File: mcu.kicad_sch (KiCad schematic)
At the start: 0 parts

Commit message: Added some components
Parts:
- added U301: STM32F413CHUx, Package_DFN_QFN:QFN-48-1EP_7x7mm_P0.5mm_EP5.6x5.6mm, symbol MCU_ST_STM32F4:STM32F413CHUx
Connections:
- new net: U301.23 (VSS), U301.35 (VSS), U301.47 (VSS), U301.49 (VSS)
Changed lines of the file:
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@@
 (kicad_sch (version 20230121) (generator eeschema)
   (paper "A4")
+  (symbol (lib_id "MCU_ST_STM32F4:STM32F413CHUx") (at 114.935 95.885 0) (unit 1)
+    (in_bom yes) (on_board yes) (dnp no) (fields_autoplaced)
+    (property "Reference" "U301" (at 119.6691 135.89 0)
+      (effects (font (size 1.27 1.27)) (justify left))
+    )
+    (property "Value" "STM32F413CHUx" (at 119.6691 138.43 0)
+      (effects (font (size 1.27 1.27)) (justify left))
+    )
+    (property "Footprint" "Package_DFN_QFN:QFN-48-1EP_7x7mm_P0.5mm_EP5.6x5.6mm" (at 102.235 133.985 0)
+      (effects (font (size 1.27 1.27)) (justify right) hide)
+    )
+    (property "Datasheet" "https://www.st.com/resource/en/datasheet/stm32f413ch.pdf" (at 114.935 95.885 0)
+      (effects (font (size 1.27 1.27)) hide)
+    )
+    (pin "1")
+    (pin "10")
+    (pin "11")
+    (pin "12")
+    (pin "13")
+    (pin "14")
+    (pin "15")
+    (pin "16")
+    (pin "17")
+    (pin "18")
+    (pin "19")
+    (pin "2")
+    (pin "20")
+    (pin "21")
+    (pin "22")
+    (pin "23")
+    (pin "24")
+    (pin "25")
+    (pin "26")
+    (pin "27")
+    (pin "28")
+    (pin "29")
+    (pin "3")
+    (pin "30")
+    (pin "31")
+    (pin "32")
+    (pin "33")
+    (pin "34")
+    (pin "35")
+    (pin "36")
+    (pin "37")
+    (pin "38")
+    (pin "39")
+    (pin "4")
+    (pin "40")
+    (pin "41")
+    (pin "42")
+    (pin "43")
+    (pin "44")
+    (pin "45")
+    (pin "46")
+    (pin "47")
+    (pin "48")
+    (pin "49")
+    (pin "5")
+    (pin "6")
+    (pin "7")
+    (pin "8")
+    (pin "9")
+    (instances
+      (project "MicroQuad"
+        (path "/8971f876-5b3c-4165-aa17-84d4a3cd004e/08fad0dd-ed56-4156-8d36-1884874d31b0"
+          (reference "U301") (unit 1)
+        )
+      )
+    )
+  )
 )

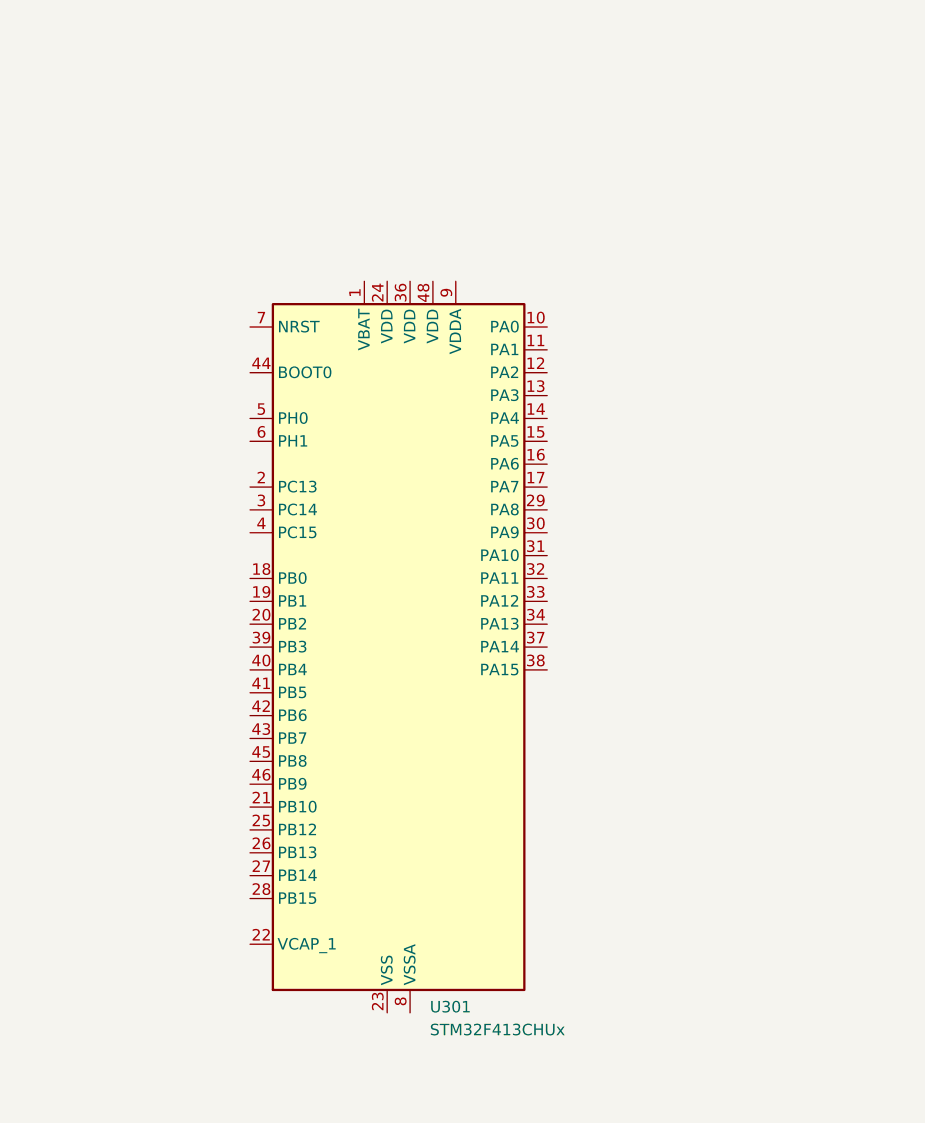
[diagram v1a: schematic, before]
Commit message: Added typical components around mcu
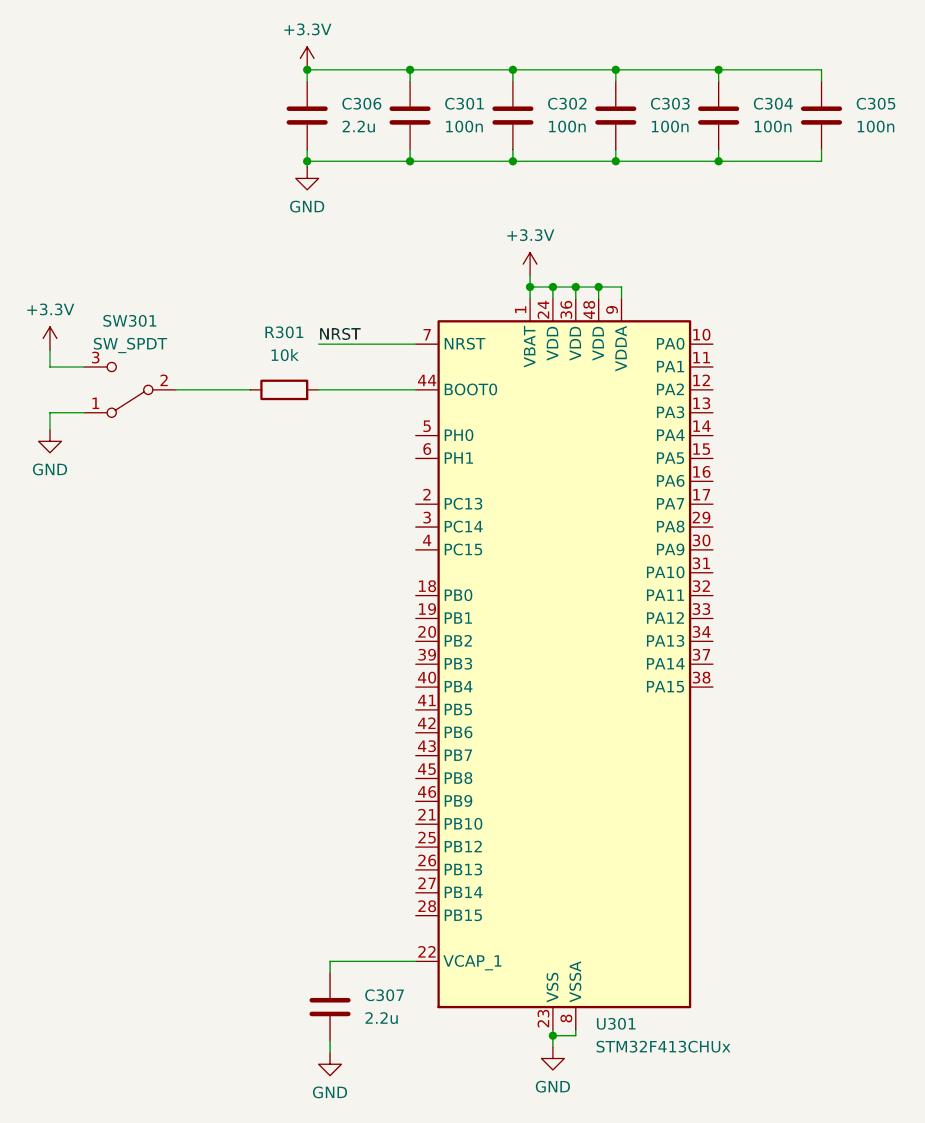
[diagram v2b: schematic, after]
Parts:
- added C301, C302, C303, C304, C305: 100n, symbol Device:C
- added C306, C307: 2.2u, symbol Device:C
- added R301: 10k, symbol Device:R
- added SW301: SW_SPDT, symbol Switch:SW_SPDT
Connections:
- net +3.3V: now reaches U301.1 (VBAT)
- net +3.3V: now also U301.24 (VDD), U301.36 (VDD), U301.48 (VDD), U301.9 (VDDA), C301.1, C302.1, C303.1, C304.1, C305.1, C306.1, SW301.3 (C)
- net at U301.22 (VCAP_1): now also C307.1
- net GND: now reaches U301.23 (VSS), U301.35 (VSS), U301.47 (VSS), U301.49 (VSS)
- net GND: now also U301.8 (VSSA), C301.2, C302.2, C303.2, C304.2, C305.2, C306.2, C307.2, SW301.1 (A)
- net at U301.44 (BOOT0): now also R301.2
- net NRST: now reaches U301.7 (NRST)
- new net: R301.1, SW301.2 (B)
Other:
- moved on the sheet: U301

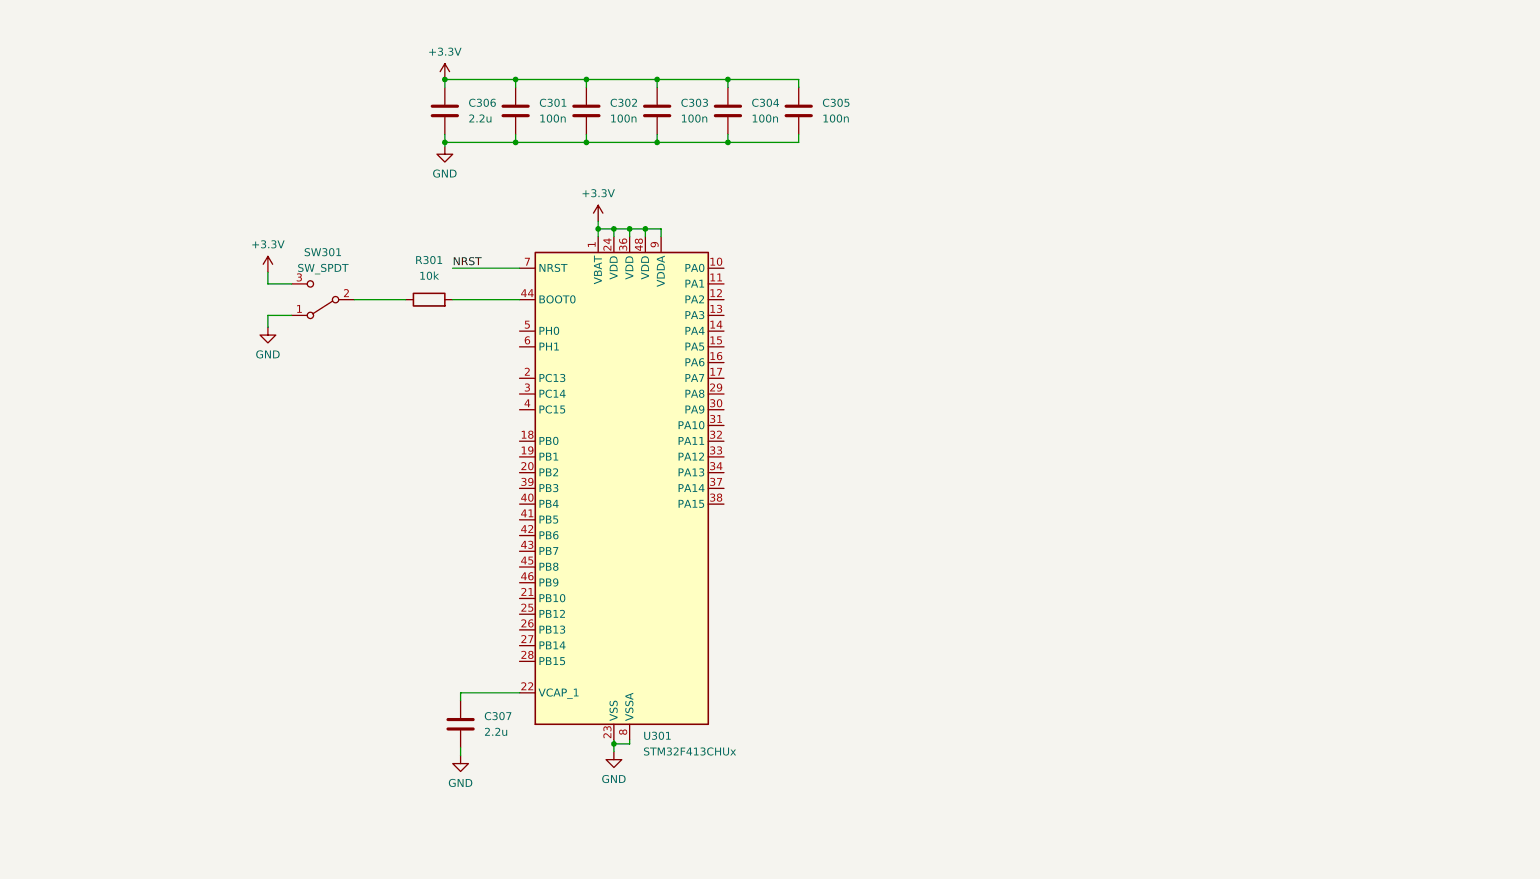
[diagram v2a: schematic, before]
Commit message: Added usb connector
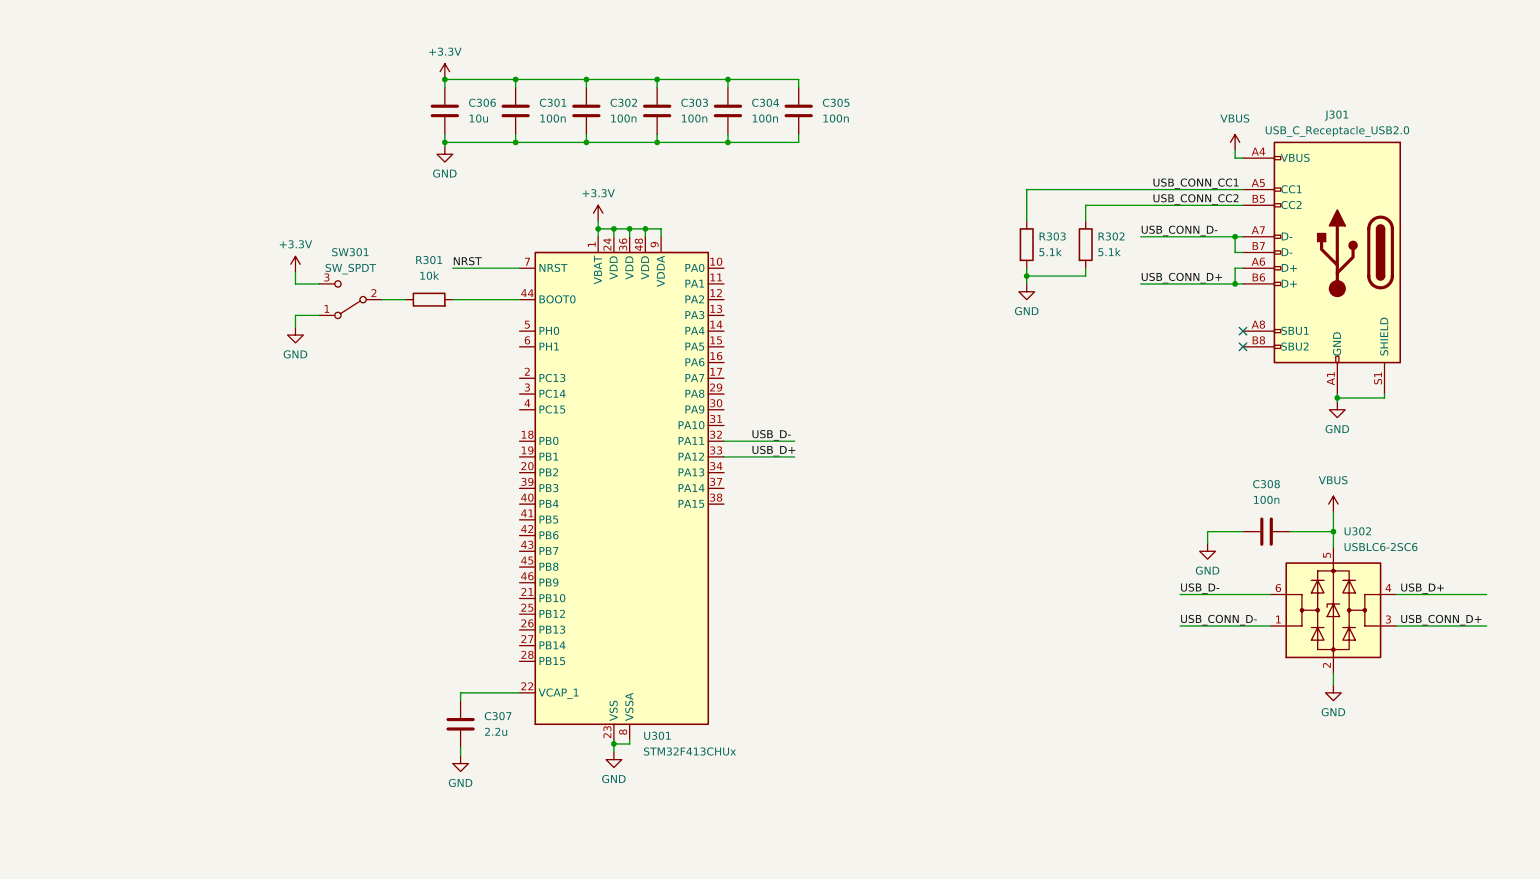
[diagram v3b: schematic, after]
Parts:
- added C308: 100n, symbol Device:C
- added J301: USB_C_Receptacle_USB2.0, symbol Connector:USB_C_Receptacle_USB2.0
- added R302, R303: 5.1k, symbol Device:R
- added U302: USBLC6-2SC6, Package_TO_SOT_SMD:SOT-23-6, symbol Power_Protection:USBLC6-2SC6
- C306: value 2.2u -> 10u
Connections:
- net GND: now also C308.1, J301.A1 (GND), J301.A12 (GND), J301.B1 (GND), J301.B12 (GND), J301.S1 (SHIELD), R302.2, R303.2, U302.2 (GND)
- net USB_D-: now reaches U301.32 (PA11)
- net USB_D-: now also U302.6 (I/O1)
- net USB_D+: now reaches U301.33 (PA12)
- net USB_D+: now also U302.4 (I/O2)
- new net USB_CONN_CC1: J301.A5 (CC1), R303.1
- new net USB_CONN_CC2: J301.B5 (CC2), R302.1
- new net USB_CONN_D+: J301.A6 (D+), J301.B6 (D+), U302.3 (I/O2)
- new net USB_CONN_D-: J301.A7 (D-), J301.B7 (D-), U302.1 (I/O1)
- new net VBUS: C308.2, J301.A4 (VBUS), J301.A9 (VBUS), J301.B4 (VBUS), J301.B9 (VBUS), U302.5 (VBUS)
- no-connect marks 0 -> 2
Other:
- moved on the sheet: SW301

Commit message: SWD and HSE
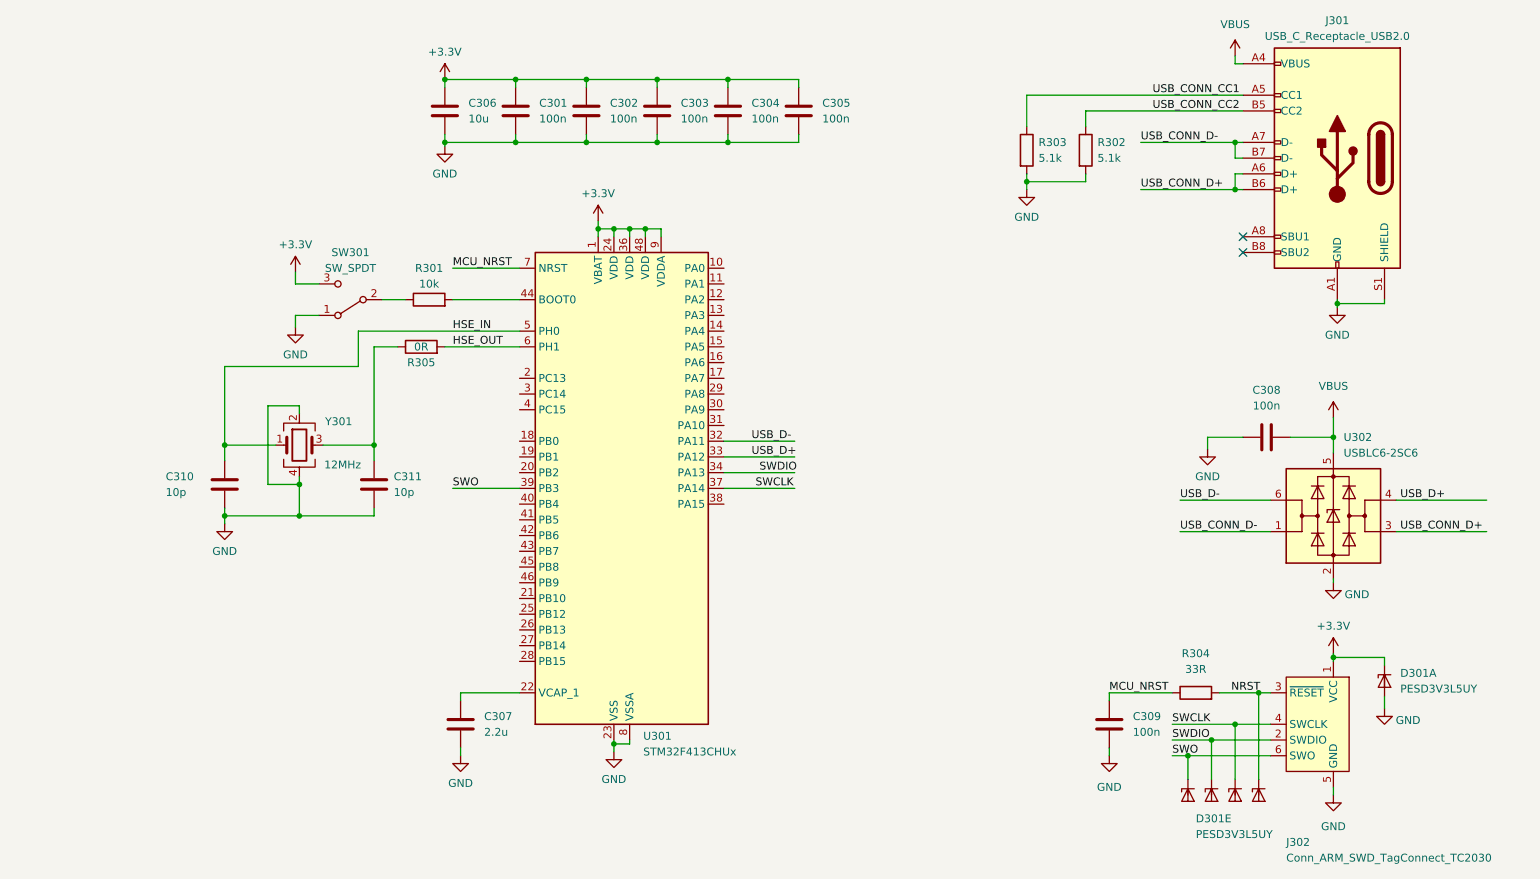
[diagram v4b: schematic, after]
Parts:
- added C309: 100n, symbol Device:C
- added C310, C311: 10p, symbol Device:C
- added D301: PESD3V3L5UY, Package_TO_SOT_SMD:SOT-363_SC-70-6, symbol Power_Protection:PESD3V3L5UY
- added J302: Conn_ARM_SWD_TagConnect_TC2030, Connector:Tag-Connect_TC2030-IDC-FP_2x03_P1.27mm_Vertical, symbol Connector:Conn_ARM_SWD_TagConnect_TC2030
- added R304: 33R, symbol Device:R
- added R305: 0R, symbol Device:R
- added Y301: 12MHz, symbol Device:Crystal_GND24
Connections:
- net +3.3V: now also D301.1 (K1), J302.1 (VCC)
- net GND: now also C309.2, C310.2, C311.2, D301.2 (A), J302.5 (GND), Y301.2, Y301.4
- net NRST: now also D301.6 (K5), J302.3 (~{RESET}), R304.2; no longer U301.7 (NRST)
- net SWDIO: now reaches U301.34 (PA13)
- net SWDIO: now also D301.4 (K3), J302.2 (SWDIO)
- net SWCLK: now reaches U301.37 (PA14)
- net SWCLK: now also D301.5 (K4), J302.4 (SWCLK)
- net SWO: now reaches U301.39 (PB3)
- net SWO: now also D301.3 (K2), J302.6 (SWO)
- net HSE_IN: now reaches U301.5 (PH0)
- net HSE_IN: now also C310.1, Y301.1
- net HSE_OUT: now reaches U301.6 (PH1)
- net HSE_OUT: now also R305.2
- new net: C311.1, R305.1, Y301.3
- new net MCU_NRST: C309.1, R304.1, U301.7 (NRST)
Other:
- moved on the sheet: C308, J301, R302, R303, U302

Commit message: Finished wiring for barometer
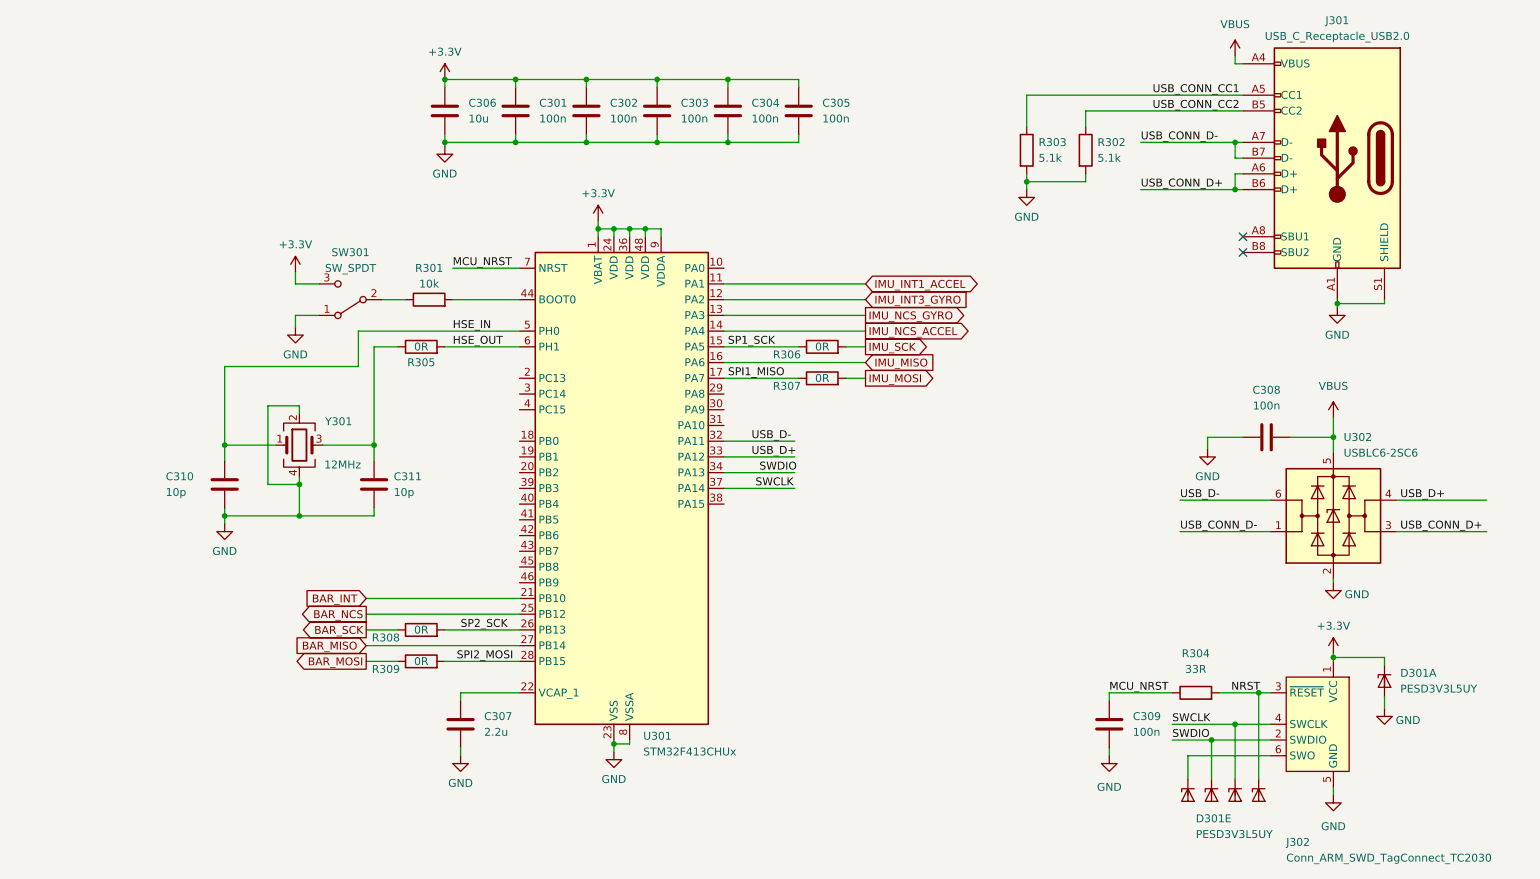
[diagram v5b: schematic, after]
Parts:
- added R306, R307, R308, R309: 0R, symbol Device:R
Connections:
- net IMU_INT1_ACCEL: now reaches U301.11 (PA1)
- net IMU_INT3_GYRO: now reaches U301.12 (PA2)
- net IMU_NCS_GYRO: now reaches U301.13 (PA3)
- net IMU_NCS_ACCEL: now reaches U301.14 (PA4)
- net SP1_SCK: now reaches U301.15 (PA5)
- net SP1_SCK: now also R306.1
- net IMU_MISO: now reaches U301.16 (PA6)
- net SPI1_MISO: now reaches U301.17 (PA7)
- net SPI1_MISO: now also R307.1
- net BAR_INT: now reaches U301.21 (PB10)
- net BAR_NCS: now reaches U301.25 (PB12)
- net SP2_SCK: now reaches U301.26 (PB13)
- net SP2_SCK: now also R308.2
- net BAR_MISO: now reaches U301.27 (PB14)
- net SPI2_MOSI: now reaches U301.28 (PB15)
- net SPI2_MOSI: now also R309.2
- net SWO: no longer names the net of D301.3 (K2), J302.6 (SWO)
- net SWO: no longer U301.39 (PB3)
- new net BAR_MOSI: R309.1
- new net BAR_SCK: R308.1
- new net IMU_MOSI: R307.2
- new net IMU_SCK: R306.2

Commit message: Added magnetometer circuitry
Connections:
- net MAG_SCL: now reaches U301.42 (PB6)
- net MAG_SDA: now reaches U301.43 (PB7)
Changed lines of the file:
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@@
+    (stroke (width 0) (type default))
+  )
+  (wire (pts (xy 107.315 107.95) (xy 118.11 107.95))
     (stroke (width 0) (type default))
   )
@@
     (stroke (width 0) (type default))
   )
+  (wire (pts (xy 107.315 105.41) (xy 118.11 105.41))
+    (stroke (width 0) (type default))
+  )
   (wire (pts (xy 128.905 31.75) (xy 140.335 31.75))
     (stroke (width 0) (type default))
@@
     )
   )
+  (global_label "MAG_SDA" (shape bidirectional) (at 107.315 107.95 180) (fields_autoplaced)
+    (effects (font (size 1.27 1.27)) (justify right))
+    (property "Intersheetrefs" "${INTERSHEET_REFS}" (at 94.8728 107.95 0)
+      (effects (font (size 1.27 1.27)) (justify right) hide)
+    )
+  )
   (global_label "IMU_NCS_ACCEL" (shape output) (at 173.99 72.39 0) (fields_autoplaced)
     (effects (font (size 1.27 1.27)) (justify left))
@@
     )
   )
+  (global_label "MAG_SCL" (shape output) (at 107.315 105.41 180) (fields_autoplaced)
+    (effects (font (size 1.27 1.27)) (justify right))
+    (property "Intersheetrefs" "${INTERSHEET_REFS}" (at 96.0446 105.41 0)
+      (effects (font (size 1.27 1.27)) (justify right) hide)
+    )
+  )
